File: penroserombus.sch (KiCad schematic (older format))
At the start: 11 parts, among them SW1 SW_DPDT_x2

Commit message: ok third time is a charm
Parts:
- renumbered JA to J1, JG to J2, JT to J3, JC to J4
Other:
- moved on the sheet: C1, C2, D1, D2, J1, J2, J3, J4

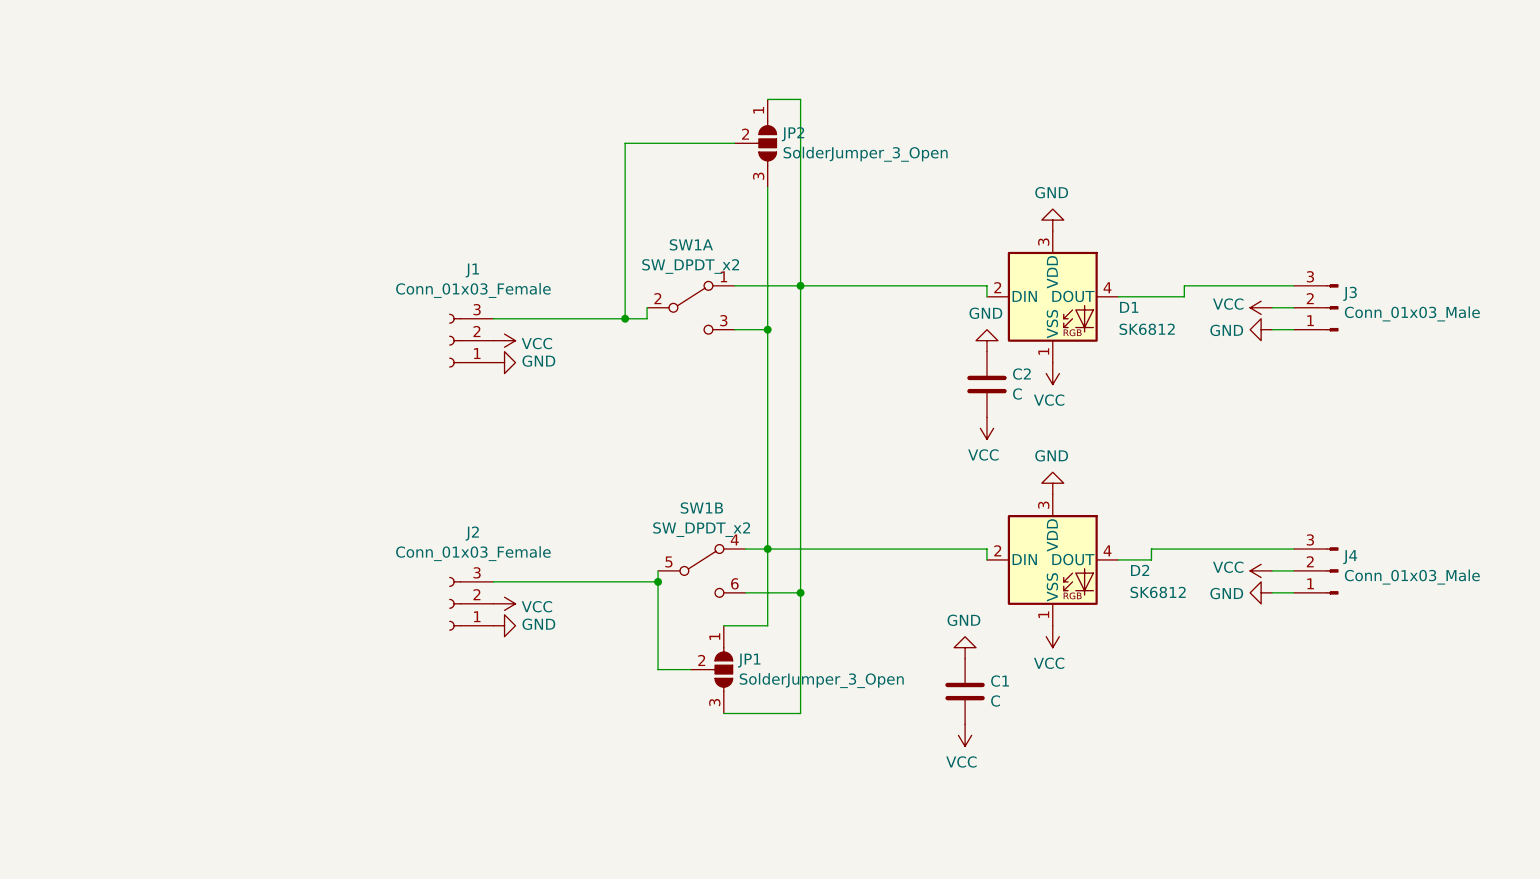
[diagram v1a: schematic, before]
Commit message: changed out 5050 leds for 2020 led
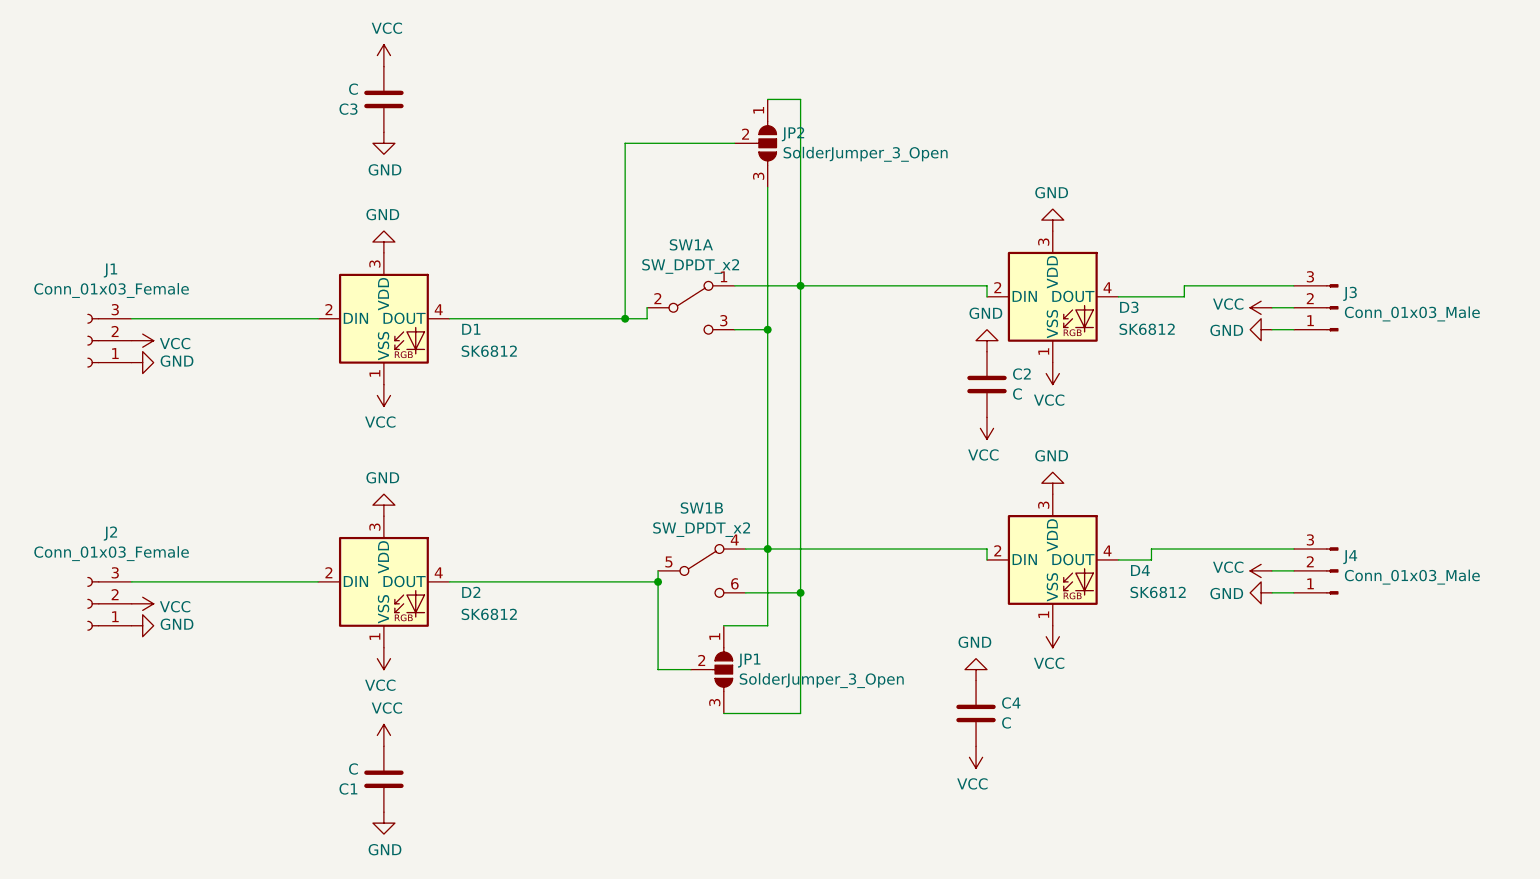
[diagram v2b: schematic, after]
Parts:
- added C3, C4: C, Capacitor_SMD:C_0805_2012Metric_Pad1.18x1.45mm_HandSolder, symbol Device:C
- added D1, D2: SK6812, penroserombus:SK6812_2020_LED, symbol LED:SK6812
- D3: renamed from D1; footprint LED_SMD:LED_SK6812_PLCC4_5.0x5.0mm_P3.2mm -> penroserombus:SK6812_2020_LED
- D4: renamed from D2; footprint LED_SMD:LED_SK6812_PLCC4_5.0x5.0mm_P3.2mm -> penroserombus:SK6812_2020_LED
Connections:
- net GND: now also C3.1, C4.1, D1.3 (VDD), D2.3 (VDD)
- net VCC: now also C3.2, C4.2, D1.1 (VSS), D2.1 (VSS)
- net at JP1.2 (C), SW1.5 (B): now also D2.4 (DOUT); no longer J2.3 (Pin_3)
- net at JP2.2 (C), SW1.2 (B): now also D1.4 (DOUT); no longer J1.3 (Pin_3)
- new net: D2.2 (DIN), J2.3 (Pin_3)
- new net: D1.2 (DIN), J1.3 (Pin_3)
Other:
- moved on the sheet: C1, J1, J2
